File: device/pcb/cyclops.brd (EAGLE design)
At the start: 124.5 x 79.9 mm, 191 parts, among them Q1 NDS351AN, Q2 NDS351AN, Q3 NDS351AN, Q4 IRF510, U1 MCP4921, U10 DG9421, U11 THS4281, U12 MAX4564, U13 ZXTD, U14 ZXTD, U15 OPA1664, U16 LTM8020, U17 DG9421, U2 LT1931, U3 LT1764A, U4 BD00FC0WEFJ, U5 TPS72325, U6 LT1711, U7 TLV3701, U8 ADR03, U9 LT1880

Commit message: Fix silkscreen.
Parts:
- removed BWFULL<>BWLIM: JS102, cyclops:JS102011SAQN
- removed D7: 1N5819, jonnew:SOD123
- removed J_ADDR0, J_CS0, J_OC0, J_T0: 0, jonnew:0402
- removed R56: 165k, cyclops:0603
- added D1: 1N5819, jonnew:SOD123
- added J_ADDR4, J_CS4, J_OC4, J_T4: 0, jonnew:0402
- added LIM<BW>FULL: JS102, cyclops:JS102011SAQN
- added R51: 220k, cyclops:0603
- C10: value 100uF -> JMK212BJ106; device cyclops:153CLV-0807 -> jonnew:0805
- C11: value 22uF -> TMK212AB7475KG-T; device cyclops:1210 -> jonnew:0805
- C12: value 10uF -> 1uF; device jonnew:1206 -> cyclops:1206
- C13: value 10uF -> 220pF; device jonnew:1206 -> cyclops:0603
- C14: value 10uF -> 4.7uF; device jonnew:1206 -> cyclops:1206
- C15: value 10nF -> 10uF; device jonnew:0603 -> jonnew:1206
- C16: value 10uF -> 10nF; device jonnew:1206 -> jonnew:0603
- C17: value .1uF -> 10uF; device cyclops:0603 -> jonnew:1206
- C18: value .1uF -> 22uF; device cyclops:0603 -> cyclops:1210
- C2: value (none) -> 10uF; device cyclops:0603 -> cyclops:1206
- C22, C25: value 1uF -> .1uF; device cyclops:0805 -> cyclops:0603
- C24: value .1uF -> 10nF
- C26, C27, C45: value 0.1uF -> 1uF; device cyclops:0603 -> cyclops:0805
- C28: value 0.1uF -> .1uF
- C3: value 10uF -> .1uF; device cyclops:1206 -> cyclops:0603
- C30, C35: value .1uF -> 10uF; device cyclops:0603 -> cyclops:1206
- C31: value 1uF -> 0.1uF; device cyclops:0805 -> cyclops:0603
- C32: value 1uF -> 100pF; device cyclops:0805 -> cyclops:0603
- C33, C39: value 10nF -> 0.1uF
- C37: value 10uF -> 0.1uF; device cyclops:1206 -> cyclops:0603
- C38: value 10uF -> 6.8nF; device cyclops:1206 -> cyclops:0603
- C4: value .1uF -> 1uF; device cyclops:0603 -> cyclops:0805
- C40: value JMK212BJ106 -> 10nF; device jonnew:0805 -> cyclops:0603
- C41: value TMK212AB7475KG-T -> 10nF; device jonnew:0805 -> cyclops:0603
- C42: value 100pF -> .1uF
- C43: value 10nF -> 1uF; device cyclops:0603 -> cyclops:0805
- C44: value 6.8nF -> .1uF
- C5: value 1uF -> (none); device cyclops:0805 -> cyclops:0603
- C6: value 4.7uF -> 10uF; device cyclops:1206 -> jonnew:1206
- C7: value 100uF -> 10uF; device cyclops:153CLV-0807 -> jonnew:1206
- C8: value 1uF -> 100uF; device cyclops:1206 -> cyclops:153CLV-0807
- C9: value 220pF -> 100uF; device cyclops:0603 -> cyclops:153CLV-0807
- D2: value 1N5819 -> SZMM3Z5V1; device jonnew:SOD123 -> cyclops:SOD-323
- D3: value SZMM3Z5V1 -> STPS0560Z; device cyclops:SOD-323 -> jonnew:SOD123
- D4: value MBR0520L -> STPS0560Z; device cyclops:SOD123 -> jonnew:SOD123
- D5: value STPS0560Z -> 1N5819
- D6: value STPS0560Z -> MBR0520L; device jonnew:SOD123 -> cyclops:SOD123
- R1: value 100k -> 10k
- R10: value 100 -> 10k; device jonnew:0603 -> cyclops:0603
- R11: value 29.4k -> 33k
- R12: value 10k -> 2.2k
- R13: value 10k -> 4.7k
- R15: value 2.2k -> 100k
- R16: value 10k -> 1M
- R17: value 40k -> 165k
- R18: value 100k -> 29.4k
- R19: value 100 -> 10k
- R2: value 10k -> (none)
- R21, R24: value 100k -> 1k
- R26, R30: value 1k -> 100k
- R27: value 1k -> 40k
- R28: value 1k -> 10k
- R3: value 10k -> 100k
- R31: value 470 -> 1k
- R32, R34: value 1k -> 100
- R35: value 220k -> 100k
- R36: value 0 -> 470
- R37: value 0 -> 1k
- R38: value 2.1k -> 1k
- R39, R50: value (none) -> 1k
- R4: value 50 -> 10k; device jonnew:1206 -> cyclops:0603
- R40: value 1k -> 0
- R41: value 220k -> 1k
- R42: value 50 -> (none)
- R44: value (none) -> 0.5
- R46: value 1k -> 50
- R48: value 0.5 -> 2.1k
- R49: value 0 -> 220k
- R5: value 33k -> 10k
- R52: value 4.7k -> 0
- R53: value 100 -> 0
- R54: value 100k -> (none)
- R55: value 1M -> (none)
- R6: value 50 -> 100; device jonnew:1206 -> jonnew:0603
- R8: value 10k -> 50; device cyclops:0603 -> jonnew:1206
- R9: value (none) -> 50; device cyclops:0603 -> jonnew:1206
- U10: value DG9421 -> LT1880; device jonnew:SOT23-6 -> jonnew:SOT95P310X175-5N
- U11: value THS4281 -> ZXTD; device jonnew:SOT95P310X175-5N -> cyclops:SOT23-6
- U12: value MAX4564 -> DG9421; device cyclops:SOT65P300X175-N -> jonnew:SOT23-6
- U13: value ZXTD -> THS4281; device cyclops:SOT23-6 -> jonnew:SOT95P310X175-5N
- U15: value OPA1664 -> DG9421; device jonnew:SO14 -> jonnew:SOT23-6
- U16: value LTM8020 -> MAX4564; device jonnew:LGA21C127P5X5_625X625X242 -> cyclops:SOT65P300X175-N
- U17: value DG9421 -> OPA1664; device jonnew:SOT23-6 -> jonnew:SO14
- U2: value LT1931 -> LT1764A; device cyclops:SOT95P310X175-5N -> cyclops:5-DDPAK
- U3: value LT1764A -> BD00FC0WEFJ; device cyclops:5-DDPAK -> jonnew:SOIC127P600X175-9N
- U4: value BD00FC0WEFJ -> LTM8020; device jonnew:SOIC127P600X175-9N -> jonnew:LGA21C127P5X5_625X625X242
- U5: value TPS72325 -> LT1931; device jonnew:SOT-23-5 -> cyclops:SOT95P310X175-5N
- U6: value LT1711 -> TPS72325; device jonnew:SOP65P490X110-8N -> jonnew:SOT-23-5
- U8: value ADR03 -> LT1711; device cyclops:SOT65P210X110-5N -> jonnew:SOP65P490X110-8N
- U9: value LT1880 -> ADR03; device jonnew:SOT95P310X175-5N -> cyclops:SOT65P210X110-5N
- moved R9 89.8 mm to (111.0, 67.4), turned to 180 degrees
- moved C9 87.4 mm to (107.6, 59.8), turned to 180 degrees
- moved C10 81.1 mm to (34.7, 24.1), turned to 270 degrees
- moved C8 75.8 mm to (107.7, 50.5), turned to 0 degrees
- moved R4 72.6 mm to (25.4, 16.5)
- moved R8 66.7 mm to (77.1, 67.4), turned to 180 degrees
- moved U2 65.3 mm to (91.7, 57.1), turned to 90 degrees
- moved R5 61.1 mm to (25.4, 14.2)
- moved C41 59.7 mm to (84.5, 33.4), turned to 0 degrees
- moved R10 57.0 mm to (100.8, 64.4)
- moved U16 56.1 mm to (84.8, 36.2), turned to 270 degrees
- moved U4 55.8 mm to (30.3, 23.1), turned to 0 degrees
- moved R21 53.9 mm to (10.4, 62.5), turned to 270 degrees
- moved R54 53.2 mm to (78.2, 38.1), turned to 0 degrees
- moved R30 52.1 mm to (58.7, 38.5), turned to 180 degrees
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- renumbered J_LDAC0 to J_LDAC4, J_VI0 to J_VI4, REF2V5 to REF2V1, REF5V0 to REF5V1
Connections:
- net +13.3V: now also C29.1, C30.1, C6.1, C9.+, R10.2, R12.2, R41.1, U11.1, U13.5, U2.4, U3.5, U3.8; no longer C10.+, C12.1, C34.1, C38.1, R13.2, R15.2, R45.1, U11.5, U13.1, U3.4, U4.5, U4.8
- net +15V: now also C8.+, D5.A, R15.2, R16.1, U2.1, U2.2; no longer C7.+, D7.A, R54.2, R55.1, U3.1, U3.2
- net +3V3: now also R1.2, R4.1, R5.1; no longer R2.1, R3.1, R8.2
- net +5V: now also C10.1, C14.1, D1.A, U4.A4, U4.A5, U4.B4, U4.B5, U4.C3, U4.C4, U4.C5, U5.4, U5.5; no longer C40.1, C6.1, D2.A, U16.A4, U16.A5, U16.B4, U16.B5, U16.C3, U16.C4, U16.C5, U2.4, U2.5
- net +6V: now also C26.1, C27.1, C3.1, C37.1, C40.1, C42.1, C43.1, C7.1, D3.C, LIM<BW>FULL.3, R11.2, R21.2, R22.2, R31.2, R51.2, U10.5, U12.1, U15.1, U16.2, U17.4, U3.1, U8.1, U9.3; no longer BWFULL<>BWLIM.3, C14.1, C19.1, C23.1, C24.1, C29.1, C39.1, C45.1, C5.1, D5.C, R26.2, R27.2, R30.2, R35.2, R5.2, U10.1, U12.2, U15.4, U17.1, U4.1, U6.1, U8.3, U9.5
- net -2.5V: now also C17.2, C23.1, C34.1, C39.1, C41.1, C44.1, C45.1, R49.1, R50.2, U11.3, U12.3, U13.2, U15.3, U16.6, U17.11, U6.5, U8.4; no longer C16.2, C21.1, C26.1, C27.1, C30.1, C32.1, C37.1, R41.1, R46.2, U10.3, U11.2, U12.6, U13.3, U15.11, U17.3, U5.5, U6.4
- net -5V: now also C15.2, U6.2, U6.3; no longer C13.2, U5.2, U5.3
- net ADDR0: now also J_ADDR1.2; no longer J_ADDR0.2
- net ADDR1: now also J_ADDR2.2; no longer J_ADDR1.2
- net ADDR2: now also J_ADDR3.2; no longer J_ADDR2.2
- net ADDR3: now also J_ADDR4.2; no longer J_ADDR3.2
- net COM: now also C38.1, U13.4, U16.8; no longer C44.1, U11.4, U12.8
- net COMP+: now also C19.1, R20.1; no longer C17.1, R16.1
- net CS: now also J_CS2.1, J_CS4.2; no longer J_CS0.1, J_CS2.2
- net CS0: now also J_CS2.2; no longer J_CS0.2
- net CS2: now also J_CS3.1; no longer J_CS2.1
- net CS3: now also J_CS4.1; no longer J_CS3.1
- net DACA: now also R2.2; no longer R9.2
- net GND: now also C10.2, C15.1, C16.2, C17.1, C42.2, C44.2, C7.2, C8.-, C9.-, D2.A, D4.A, D6.C, J_ADDR4.1, LIM<BW>FULL.1, R13.1, R16.2, R17.1, R26.1, R28.2, R35.1, R38.2, R39.1, R42.2, R54.2, U12.2, U15.2, U16.5, U16.7, U2.3, U2.TAB, U3.4, U3.6, U3.7, U3.9, U4.C2, U4.D1, U4.D2, U4.D3, U4.D4, U4.D5, U4.E2, U4.E3, U4.E4, U4.E5, U5.2, U6.1, U8.5, U8.6; no longer BWFULL<>BWLIM.1, C10.-, C12.2, C13.1, C15.2, C16.1, C17.2, C32.2, C38.2, C7.-, D3.A, D4.C, D6.A, J_ADDR0.1, R12.1, R20.2, R24.1, R29.1, R33.2, R39.2, R44.2, R50.2, R52.1, R56.1, U12.5, U12.7, U16.C2, U16.D1, U16.D2, U16.D3, U16.D4, U16.D5, U16.E2, U16.E3, U16.E4, U16.E5, U17.2, U2.2, U3.TAB, U4.3, U4.4, U4.6, U4.7, U4.9, U5.1, U6.5, U6.6, U8.2
- net IN: now also U16.3; no longer U12.3
- net IN1: now also LIM<BW>FULL.2, U15.6; no longer BWFULL<>BWLIM.2, U17.6
- net ISENSE: now also U16.1, U17.10, U17.3; no longer U12.1, U15.10, U15.3
- net LDAC1: now also J_LDAC3.2; no longer J_LDAC1.2
- net LDAC3: now also J_LDAC1.2; no longer J_LDAC3.2
- net LED_ACTIVE: now also R33.2, U8.8; no longer R23.2, U6.8
- net N$1: now also C5.1, R2.1; no longer C2.1, R9.1
- net N$10: now also R50.1, U11.5, U14.6; no longer R46.1, U13.6, U14.5
- net N$11: now also R53.1, R55.1, U17.2; no longer R49.1, R50.1, U15.2
- net N$12: now also R10.1, U2.5; no longer R13.1, U3.5
- net N$13: now also C32.1, R46.1, U13.1, U15.4; no longer C42.1, R42.1, U11.1, U17.4
- net N$14: now also R6.1; no longer R10.1
- net N$15: now also R52.1, R54.1, U17.9; no longer R43.1, R44.1, U15.9
- net N$16: now also C32.2, R46.2, U14.2, U14.5; no longer C42.2, R42.2, U13.2, U13.5
- net N$18: now also R37.2, R38.1, U10.4; no longer R33.1, R34.2, U9.4
- net N$2: now also R21.1; no longer R26.1
- net N$20: now also R36.2, U9.5; no longer R31.2, U8.5
- net N$21: now also C11.1, D5.C, U4.A1, U4.A2; no longer C41.1, D7.C, U16.A1, U16.A2
- net N$22: now also R36.1; no longer R31.1
- net N$23: now also R15.1, U4.C1; no longer R54.1, U16.C1
- net N$24: now also R47.1, U11.4; no longer R48.1, U14.4
- net N$25: now also R44.1, U11.6; no longer R47.1, U14.6
- net N$26: now also R44.2; no longer R48.2
- net N$27: now also R24.2; no longer R22.2
- net N$28: now also Q2.G, R24.1, R26.2; no longer Q1.G, R22.1, R24.2
- net N$3: now also R12.1; no longer R15.1
- net N$32: now also C12.1, U5.1; no longer C8.1, U2.1
- net N$33: now also C12.2, D6.A; no longer C8.2, D4.A
- net N$35: now also C13.1, C18.1, R18.2; no longer C11.1, C9.1, R11.2
- net N$36: now also C13.2, R18.1, R19.2, U5.3; no longer C9.2, R11.1, R12.2, U2.3
- net N$37: now also R45.1; no longer R40.1
- net N$38: now also R17.2, U4.E1; no longer R56.2, U16.E1
- net N$39: now also Q1.G, R23.1, R25.2; no longer Q3.G, R28.1, R29.2
- net N$4: now also R41.2, U11.2, U14.4; no longer R45.2, U13.4, U14.2
- net N$40: now also C38.2, U15.5; no longer C44.2, U17.5
- net N$41: now also Q1.D, R22.1; no longer Q3.D, R30.1
- net N$42: now also R29.1, R30.1, R32.2, U8.2; no longer R18.1, R19.2, R21.1, U6.2
- net N$43: now also R11.1, R13.2, U3.2; no longer R5.1, R52.2, U4.2
- net N$46: now also R31.1; no longer R27.1
- net N$47: now also Q3.D; no longer Q2.D
- net N$49: now also Q3.G, R33.1, R35.2; no longer Q2.G, R23.1, R25.2
- net N$5: now also C21.1, R27.2, R28.1; no longer C18.1, R17.2, R20.1
- net N$51: now also C16.1, U6.4; no longer C15.1, U5.4
- net N$52: now also R8.1; no longer R4.1
- net N$54: now also R7.1; no longer R6.1
- net N$55: now also R9.1; no longer R7.1
- net N$58: now also L2.1; no longer L1.1
- net N$6: now also R39.2; no longer R32.2
- net N$7: now also C24.1, R34.2, U8.3; no longer C43.1, R53.2, U6.3
- net N$8: now also R40.1, R42.1, U17.13; no longer R36.1, R39.1, U15.13
- net N$9: now also Q2.D; no longer Q1.D
- net REF2.5: now also C2.1, U10.3, U9.4; no longer C3.1, U8.4, U9.3
- net REF5.0: now also R27.1, R29.2, R37.1, U10.1; no longer R17.1, R18.2, R34.1, U9.1
- net SCL: now also R4.2; no longer R2.2
- net SDA: now also R5.2; no longer R3.2
- net T0: now also J_T1.1; no longer J_T0.1
- net T1: now also J_T2.1; no longer J_T1.1
- net T2: now also J_T3.1; no longer J_T2.1
- net T3: now also J_T4.1; no longer J_T3.1
- net TEENSY_VIN: now also D1.C; no longer D2.C
- net TRIG: now also J_T4.2; no longer J_T0.2
- net VAUX: now also D3.A, D4.C, R51.1, U16.4, U17.5; no longer D5.A, D6.C, R35.1, U12.4, U15.5
- net VAUX_OUT: now also R8.2, U17.6, U17.7; no longer R4.2, U15.6, U15.7
- net VCTL: now also D2.C, R43.2, R6.2, U12.4; no longer D3.C, R10.2, R37.2, U10.4
- net VCTL_PROT: now also R43.1, R48.2, U12.5; no longer R37.1, R38.2, U10.5
- net VCTL_PROTECT: now also R48.1; no longer R38.1
- net VI: now also R52.2, R7.2, U17.8; no longer R43.2, R6.2, U15.8
- net VI1: now also J_VI3.1; no longer J_VI1.1
- net VI3: now also J_VI1.1; no longer J_VI3.1
- net VI_INTERNAL: now also R20.2, R3.1, R34.1, R53.2, U17.1; no longer R1.1, R16.2, R49.2, R53.1, U15.1
- net VI_LP: now also L2.2, R3.2; no longer L1.2, R1.2
- net VREF: now also R40.2, U17.14; no longer R36.2, U15.14
- net VREF/TTL: now also R9.2; no longer R7.2
- net _VREF: now also R45.2, R49.2, U13.3, U17.12; no longer R40.2, R41.2, U11.3, U15.12
- net ~LED_ACTIVE: now also R30.2, U8.7; no longer R21.2, U6.7
- net ~OC0: now also J_OC1.2; no longer J_OC0.2
- net ~OC1: now also J_OC2.2; no longer J_OC1.2
- net ~OC2: now also J_OC4.2; no longer J_OC2.2
- net ~OVER_CURR: now also L1.1, U12.6; no longer L2.1, U10.6
- net ~OVER_CURR_PRE: now also J_OC4.1, L1.2, R1.1, R23.2; no longer J_OC0.1, L2.2, R28.2, R8.1
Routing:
- net IN: track 62.6 -> 42.1 mm
- net IN1: track 56.0 -> 47.5 mm
- net -2.5V: track 36.4 -> 40.5 mm
- net GND: track 112.5 -> 111.9 mm, vias 417 -> 420

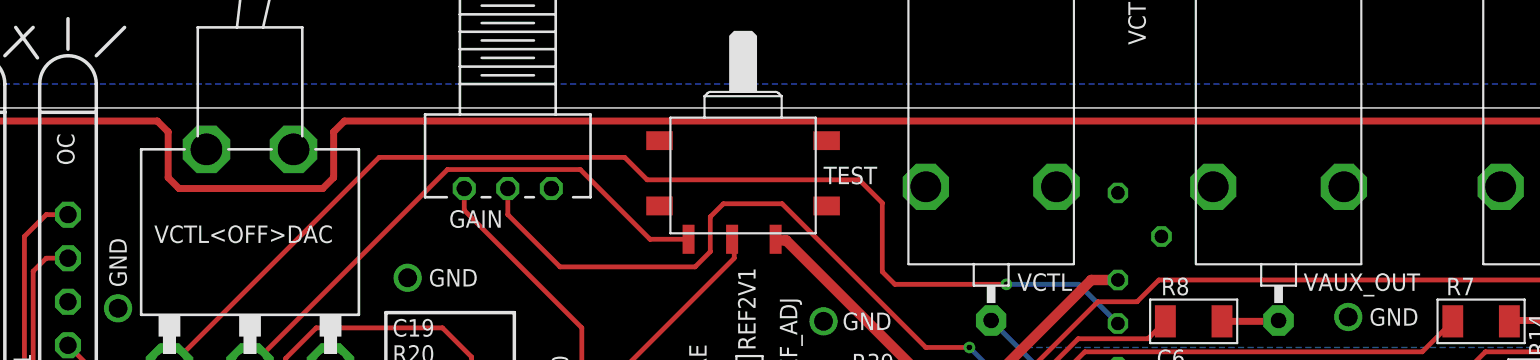
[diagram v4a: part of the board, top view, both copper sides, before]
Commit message: Panels and final protoboard sent to production.
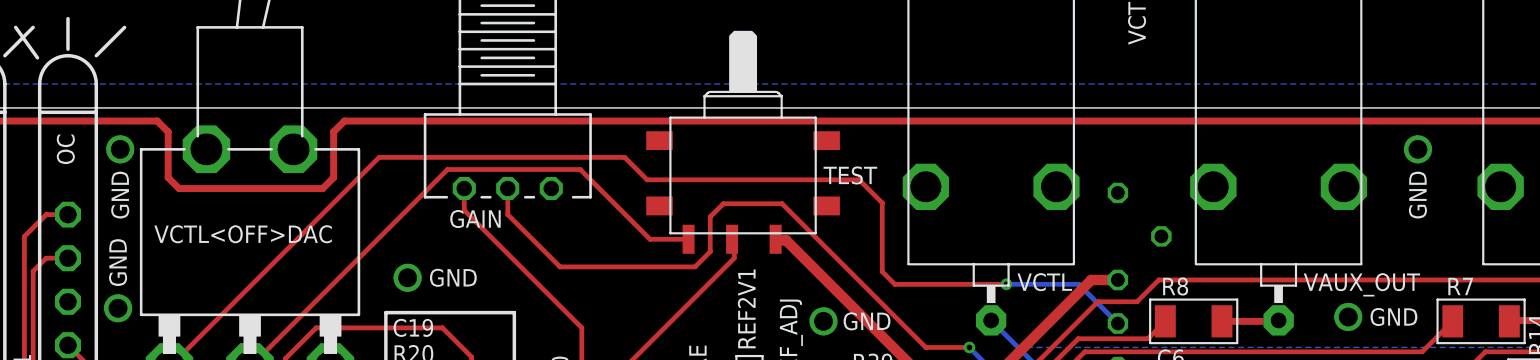
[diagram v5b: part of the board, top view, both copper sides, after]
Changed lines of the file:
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@@
 <?xml version="1.0" encoding="utf-8"?>
 <!DOCTYPE eagle SYSTEM "eagle.dtd">
-<eagle version="6.6.0">
+<eagle version="6.5.0">
 <drawing>
 <settings>
@@
 <setting verticaltext="up"/>
 </settings>
-<grid distance="0.005" unitdist="inch" unit="inch" style="lines" multiple="1" display="yes" altdistance="0.025" altunitdist="inch" altunit="inch"/>
+<grid distance="0.005" unitdist="inch" unit="mm" style="lines" multiple="1" display="yes" altdistance="0.025" altunitdist="inch" altunit="inch"/>
 <layers>
 <layer number="1" name="Top" color="4" fill="1" visible="yes" active="yes"/>
@@
 <wire x1="106.172" y1="43.561" x2="106.045" y2="43.561" width="0.2032" layer="21"/>
 <wire x1="106.172" y1="43.815" x2="106.045" y2="43.815" width="0.2032" layer="21"/>
+<text x="14.478" y="74.803" size="1.016" layer="21" font="vector" ratio="18" rot="R90" align="center">GND</text>
+<text x="90.17" y="74.803" size="1.016" layer="21" font="vector" ratio="18" rot="R90" align="center">GND</text>
 </plain>
 <attributes>
@@
 <via x="91.948" y="15.494" extent="1-16" drill="0.3302"/>
 </signal>
+<signal name="GND7">
+<via x="14.478" y="77.47" extent="1-16" drill="1.1" shape="octagon" alwaysstop="yes"/>
+</signal>
+<signal name="GND8">
+<via x="90.17" y="77.47" extent="1-16" drill="1.1" shape="octagon" alwaysstop="yes"/>
+</signal>
 </signals>

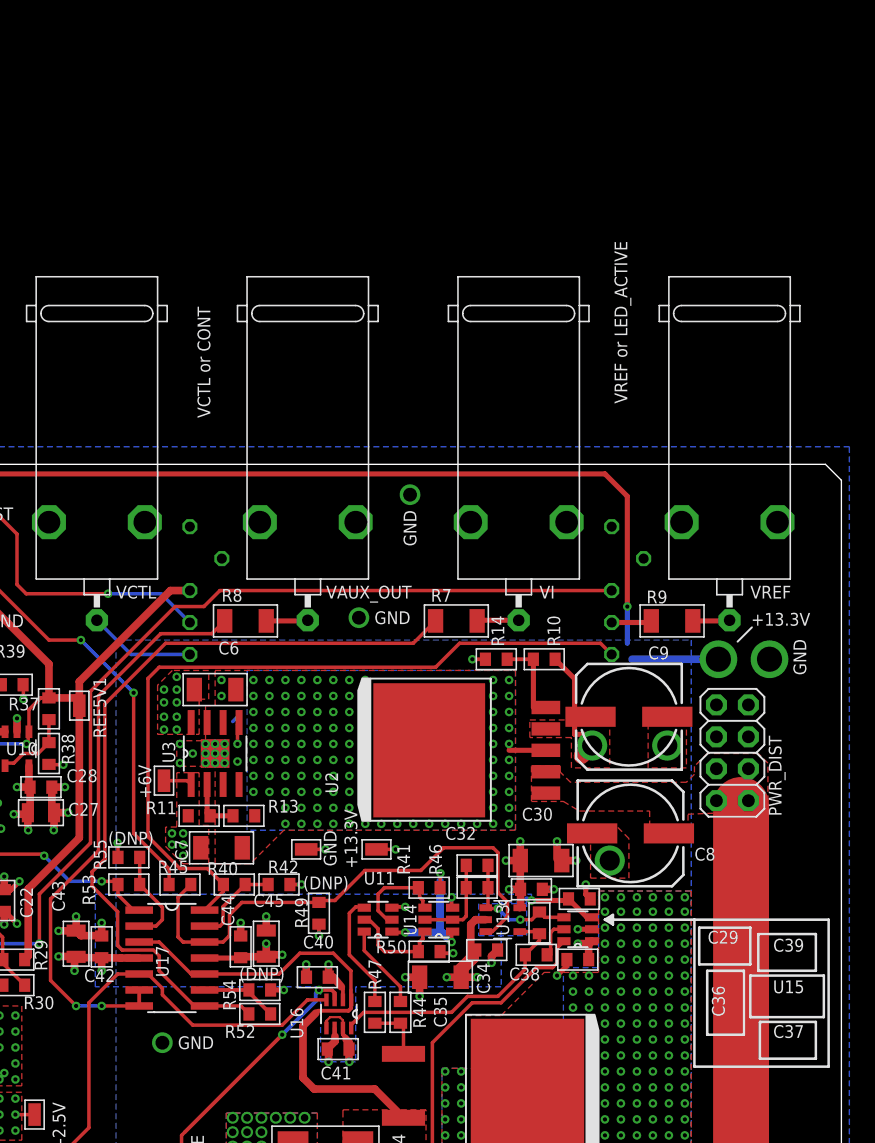
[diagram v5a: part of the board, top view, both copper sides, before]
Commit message: Minor fixes after assembly of 3.6
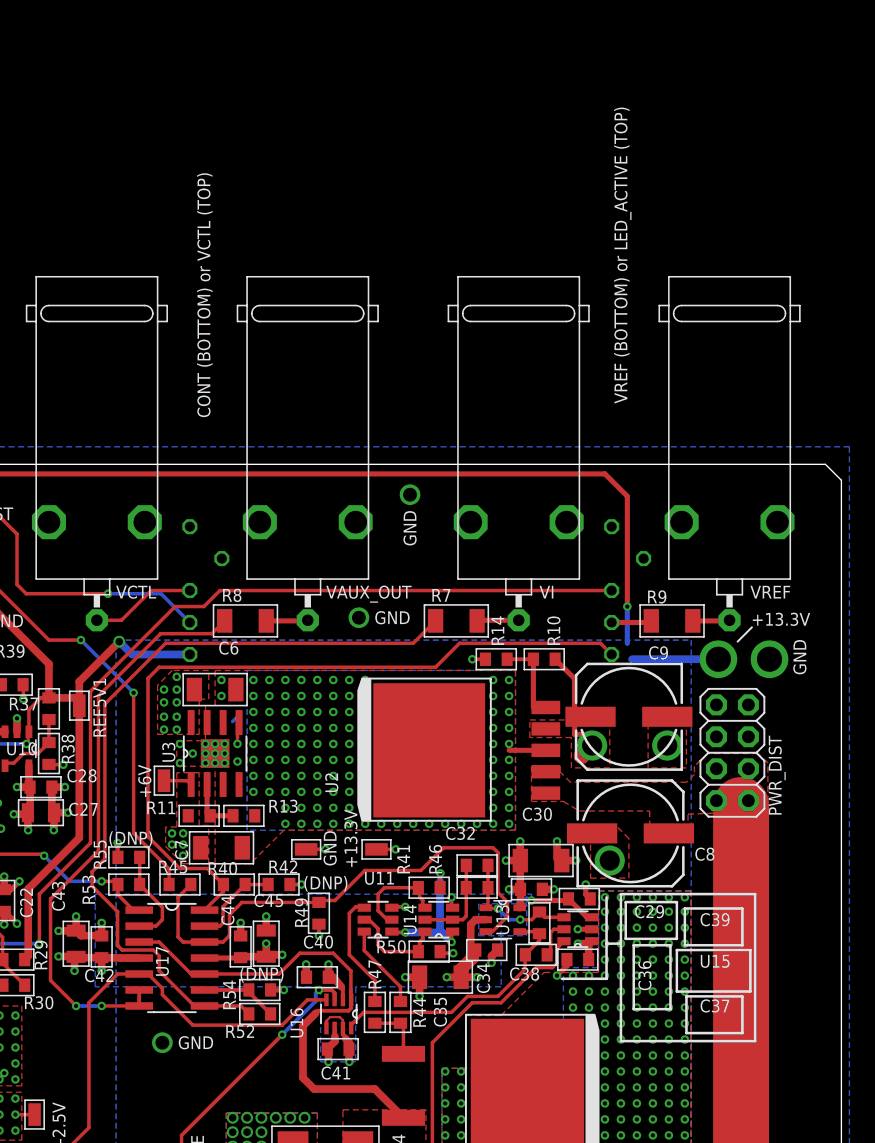
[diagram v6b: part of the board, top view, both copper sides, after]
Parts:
- R12: value 2.2k -> 2.1k
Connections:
- net N$19: now also VCTL<>CONT.P3; no longer VCTL<>CONT.P1
- net REF5.0: now also VCTL<>CONT.P1; no longer VCTL<>CONT.P3
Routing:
- net REF5.0: track 84.7 -> 83.4 mm, vias 2 -> 3
- net GND: vias 420 -> 427
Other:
- board text added: "CONT (BOTTOM) or VCTL (TOP)"
- board text added: "VREF (BOTTOM) or LED_ACTIVE (TOP)"
- board text removed: "VCTL or CONT"
- board text removed: "VREF or LED_ACTIVE"
